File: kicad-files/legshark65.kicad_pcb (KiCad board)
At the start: 2 copper layers, 130 parts

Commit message: Update schematic to noLED MX only footpints
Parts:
- moved K_12 14.1 mm to (258.6, 30.0)
- moved K_26 14.1 mm to (258.6, 49.0)
- moved K_55 14.1 mm to (258.6, 96.7)
- moved K_41 14.1 mm to (258.6, 68.1)
- moved D_0 14.1 mm to (38.5, 30.5)
- moved D_1 14.1 mm to (57.6, 30.5)
- moved D_10 14.1 mm to (229.0, 30.5)
- moved D_11 14.1 mm to (248.1, 30.5)
- moved D_12 14.1 mm to (267.1, 30.5)
- moved D_13 14.1 mm to (286.2, 30.5)
- moved D_14 14.1 mm to (305.2, 30.5)
- moved D_15 14.1 mm to (57.6, 49.5)
- moved D_16 14.1 mm to (76.6, 49.5)
- moved D_17 14.1 mm to (95.7, 49.5)
- moved D_18 14.1 mm to (114.7, 49.5)
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
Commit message: Updated PCB design constraints
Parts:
- added C1: 15p, Capacitor_SMD:C_0603_1608Metric_Pad1.08x0.95mm_HandSolder, B.Cu at (245.9, 74.8)
- added C10: 100n, Capacitor_SMD:C_0603_1608Metric_Pad1.08x0.95mm_HandSolder, B.Cu at (153.6, 145.7)
- added C11: 100n, Capacitor_SMD:C_0603_1608Metric_Pad1.08x0.95mm_HandSolder, B.Cu at (153.6, 148.2)
- added C12: 10n, Capacitor_SMD:C_0603_1608Metric_Pad1.08x0.95mm_HandSolder, B.Cu at (153.6, 150.7)
- added C13: 4.7u, Capacitor_SMD:C_0603_1608Metric_Pad1.08x0.95mm_HandSolder, B.Cu at (149.2, 143.2)
- added C14: 100n, Capacitor_SMD:C_0603_1608Metric_Pad1.08x0.95mm_HandSolder, B.Cu at (149.2, 145.7)
- added C15: 4.7u, Capacitor_SMD:C_0603_1608Metric_Pad1.08x0.95mm_HandSolder, B.Cu at (149.2, 148.2)
- added C16: 16V 10uF Tantallum, acheron_Components:CP_EIA-3216-10_Kemet-I_Pad1.58x1.35mm_HandSolder, B.Cu at (155.1, 191.1)
- added C17: 100n, Capacitor_SMD:C_0603_1608Metric_Pad1.08x0.95mm_HandSolder, B.Cu at (149.2, 150.7)
- added C2: 15p, Capacitor_SMD:C_0603_1608Metric_Pad1.08x0.95mm_HandSolder, B.Cu at (245.9, 80.8)
- added C6: 100n, Capacitor_SMD:C_0603_1608Metric_Pad1.08x0.95mm_HandSolder, B.Cu at (237.6, 100.0)
- added C7: 100n, Capacitor_SMD:C_0603_1608Metric_Pad1.08x0.95mm_HandSolder, B.Cu at (157.9, 150.7)
- added C9: 100n, Capacitor_SMD:C_0603_1608Metric_Pad1.08x0.95mm_HandSolder, B.Cu at (153.6, 143.2)
- added Legshark_Logo2: Huge, Legshark:Legshark_Logo_Huge, F.Cu at (-74.8, 64.1)
- added R11: 100R, Resistor_SMD:R_0603_1608Metric, B.Cu at (158.1, 138.2)
- added R15: 10k, Resistor_SMD:R_0603_1608Metric, B.Cu at (158.1, 140.7)
- added R5: 1.5k, Resistor_SMD:R_0603_1608Metric, B.Cu at (158.1, 128.1)
- added R6: 10k, Resistor_SMD:R_0603_1608Metric, B.Cu at (158.1, 130.6)
- added R7: 4.7k, Resistor_SMD:R_0603_1608Metric, B.Cu at (245.0, 100.0)
- added R8: 4.7k, Resistor_SMD:R_0603_1608Metric, B.Cu at (241.3, 100.0)
- added SW1: K2-1187SQ-A4SW-06, acheron_Hardware:K2-1187SQ-A4SW-06, B.Cu at (155.3, 180.0)
- added SW2: PCM12SMTR, Legshark:Surface Mount Slide Switch SPDT, B.Cu at (155.2, 172.8)
- added SWD1: ~, Legshark:1x02_Long_Header, B.Cu at (152.2, 194.5)
- added T2: 53261-0471, Legshark:Molex, PicoBlade, 53261, 4 Way, 1 Row, Right Angle PCB Header, B.Cu at (154.0, 154.2)
- added U1: STM32F411CEU6, acheron_Components:STM_UFQFPN-48_LQFP-48-1EP_7x7mm_P0.5mm_HandSoldering, B.Cu at (258.0, 82.0)
- added U3: AT24C256C-SSHL-T, acheron_Components:TSSOP-8_4.4x3mm_P0.65mm, B.Cu at (241.3, 97.0)
- added Y1: TAXM8M4RFDCET2T, acheron_Components:Crystal_SMD_3225-4Pin_3.2x2.5mm, B.Cu at (245.9, 77.8)
- K_0, K_1, K_10, K_11, K_12, K_13, K_14, K_16, K_17, K_18, K_19, K_2, K_20, K_21, K_22, K_23, K_24, K_25, K_26, K_27, K_28, K_29, K_3, K_30, K_31, K_32, K_33, K_34, K_35, K_36, K_37, K_38, K_39, K_4, K_40, K_41, K_44, K_45, K_46, K_47, K_48, K_49, K_5, K_50, K_51, K_52, K_53, K_54, K_55, K_56, K_6, K_64, K_7, K_8, K_9: footprint MX_Alps_Hybrid:MX-1U-NoLED -> MX_Only:MXOnly-1U-NoLED
- K_15, K_42, K_43: footprint MX_Alps_Hybrid:MX-2U-NoLED -> MX_Only:MXOnly-2U-NoLED
- K_57: footprint MX_Alps_Hybrid:MX-1.75U-NoLED -> MX_Only:MXOnly-1.75U-NoLED
- K_58, K_59, K_62, K_63: footprint MX_Alps_Hybrid:MX-1.25U-NoLED -> MX_Only:MXOnly-1.25U-NoLED
- K_60: footprint MX_Alps_Hybrid:MX-2.25U-NoLED -> MX_Only:MXOnly-2.25U-ReversedStabilizers-NoLED
- K_61: footprint MX_Alps_Hybrid:MX-3U-NoLED -> MX_Only:MXOnly-3U-ReversedStabilizers-NoLED
- moved D_22 3.85 mm to (187.6, 51.5)
- moved D_26 3.85 mm to (263.8, 51.5)
- moved D_27 3.85 mm to (282.8, 51.5)
- moved D_28 3.85 mm to (301.9, 51.5)
- moved D_37 3.85 mm to (187.6, 70.5)
- moved D_41 3.85 mm to (263.8, 70.5)
- moved D_42 3.85 mm to (301.9, 70.5)
- moved D_55 3.85 mm to (263.8, 99.1)
- moved D_56 3.85 mm to (301.9, 99.1)
- moved K_20 3.85 mm to (140.9, 51.0)
- moved K_25 3.85 mm to (236.2, 51.0)
- moved K_26 3.85 mm to (255.2, 51.0)
- moved K_35 3.85 mm to (140.9, 70.0)
- moved K_40 3.85 mm to (236.2, 70.0)
- moved K_41 3.85 mm to (255.2, 70.0)
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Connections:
- net col0 renamed c0
- net col1 renamed c1
- net col10 renamed c10
- net col11 renamed c11
- net col12 renamed c12
- net col13 renamed c13
- net col14 renamed c14
- net col2 renamed c2
- net col3 renamed c3
- net col4 renamed c4
- net col5 renamed c5
- net col6 renamed c6
- net col7 renamed c7
- net col8 renamed c8
- net col9 renamed c9
- net row0 renamed r0
- net row1 renamed r1
- net row2 renamed r2
- net row3 renamed r3
- net row4 renamed r4
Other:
- board outline added: 290 x 92 mm
- rule pad_to_mask_clearance: 0 -> 0.1

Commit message: Connected most of the rows and cols
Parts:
- moved SW1 164.3 mm to (285.5, 79.8), turned to 90 degrees
- moved SW2 157.1 mm to (264.6, 60.1), turned to 0 degrees
- moved SWD1 155.1 mm to (245.9, 70.8), turned to -90 degrees
- moved C17 143.2 mm to (264.4, 65.7)
- moved C7 141.3 mm to (278.7, 77.4), turned to -90 degrees
- moved R11 136.9 mm to (280.8, 77.5), turned to -90 degrees
- moved C16 135.0 mm to (235.6, 82.7), turned to -90 degrees
- moved R15 131.1 mm to (264.4, 64.0), turned to 0 degrees
- moved C14 130.9 mm to (264.4, 83.5)
- moved C9 126.7 mm to (264.4, 81.8)
- moved C10 124.7 mm to (256.0, 74.7), turned to -90 degrees
- moved C12 117.1 mm to (254.8, 92.0)
- moved C13 116.6 mm to (254.8, 93.9)
- moved C15 115.2 mm to (248.4, 89.7), turned to -90 degrees
- moved C11 114.7 mm to (247.8, 82.8), turned to 0 degrees
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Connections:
- T2 pad 2: D+ -> D-
- T2 pad 3: D- -> D+
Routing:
- net r0: track 0.00 -> 257.2 mm
- net r4: track 0.00 -> 253.2 mm
- net r1: track 0.00 -> 247.6 mm
- net r2: track 0.00 -> 227.0 mm
- net r3: track 0.00 -> 191.5 mm
- net c0: track 0.00 -> 80.7 mm
- net c8: track 0.00 -> 80.4 mm
- net c10: track 0.00 -> 79.4 mm
- net c3: track 0.00 -> 77.3 mm
- net c2: track 0.00 -> 77.3 mm
- net c5: track 0.00 -> 77.3 mm
- net c1: track 0.00 -> 69.4 mm
- net c9: track 0.00 -> 57.2 mm
- net c7: track 0.00 -> 57.2 mm
- net c4: track 0.00 -> 57.2 mm
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- added copper zone on B.Cu, net (none)
- added copper zone on F.Cu, net (none)

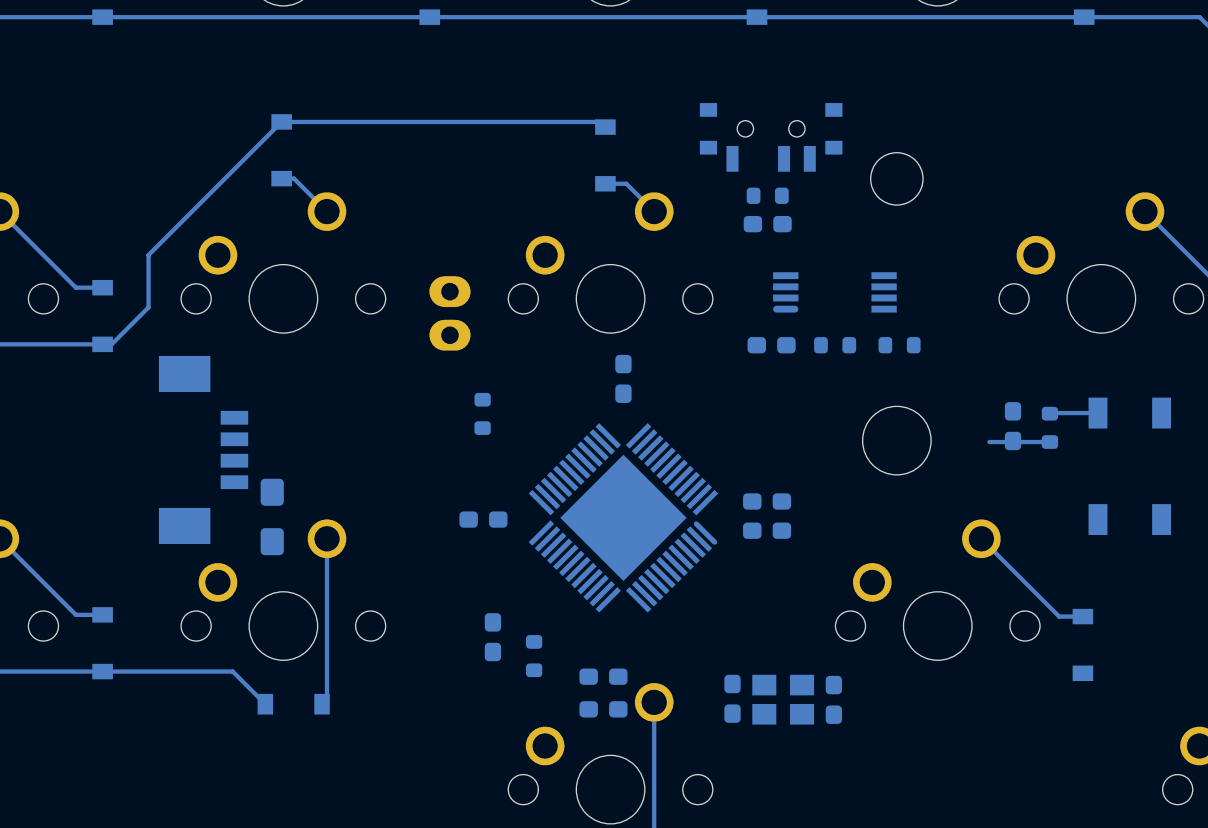
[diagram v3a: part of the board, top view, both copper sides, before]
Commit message: Started adding 3v3 pour
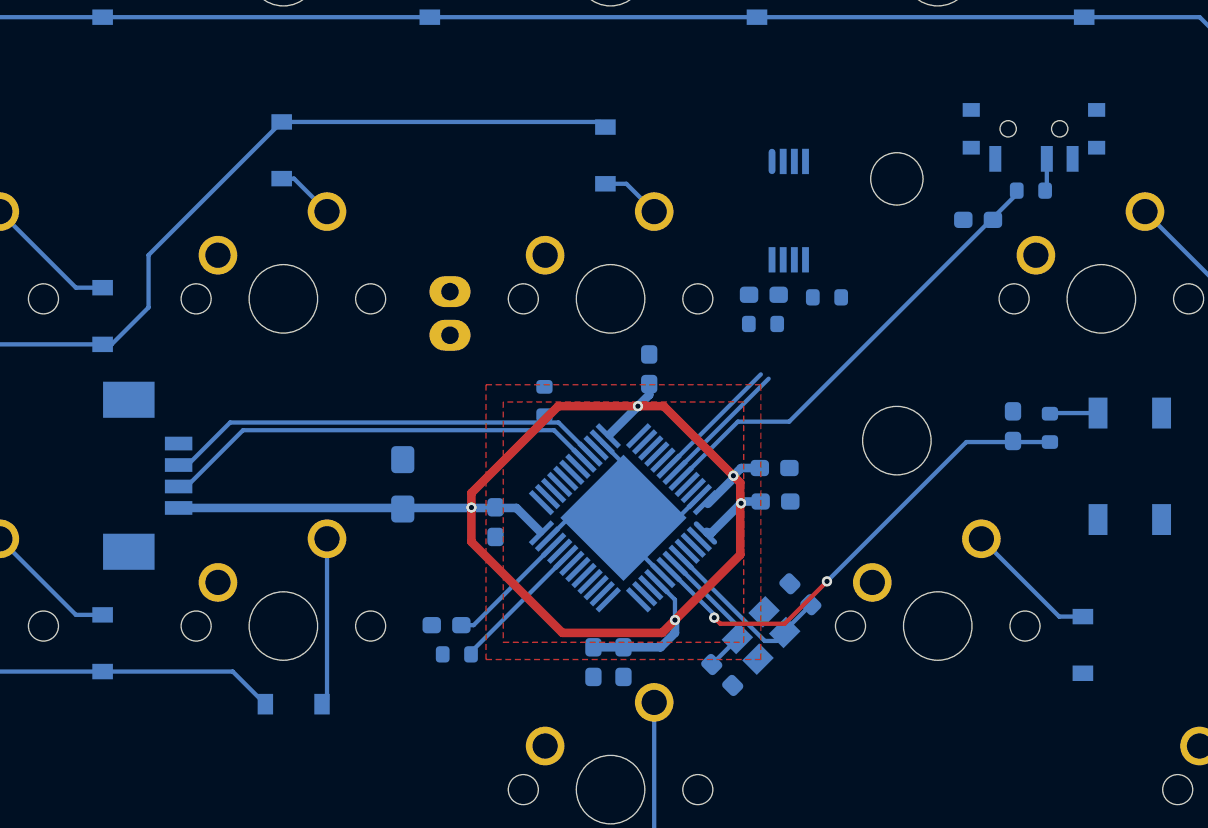
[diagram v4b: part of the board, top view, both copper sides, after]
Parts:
- moved R15 15.3 mm to (279.7, 63.7)
- moved SW2 15.3 mm to (279.9, 60.1)
- moved C17 12.3 mm to (276.6, 65.4), turned to 0 degrees
- moved C16 7.83 mm to (243.2, 80.8), turned to 90 degrees
- moved C2 6.45 mm to (266.3, 87.2), turned to 135 degrees
- moved U3 5.47 mm to (265.6, 64.9), turned to -90 degrees
- moved R7 5.06 mm to (267.9, 69.9)
- moved R6 4.50 mm to (246.3, 90.7), turned to 0 degrees
- moved R8 4.38 mm to (264.1, 71.5), turned to 0 degrees
- moved Y1 3.95 mm to (264.0, 89.6), turned to -135 degrees
- moved R5 3.68 mm to (251.4, 76.0)
- moved T2 3.58 mm to (229.3, 80.3)
- moved C6 2.97 mm to (264.2, 69.8)
- moved C13 2.81 mm to (254.2, 91.2), turned to 90 degrees
- moved C15 2.79 mm to (245.7, 89.0), turned to 180 degrees
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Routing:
- net 3V3: track 0.00 -> 88.4 mm, vias 0 -> 5
- net Net-(U1-BOOT0): track 0.00 -> 26.6 mm
- net D+: track 0.00 -> 25.2 mm
- net D-: track 0.00 -> 25.2 mm
- net Net-(U1-NRST): track 3.53 -> 28.0 mm, vias 0 -> 2
- net Net-(U1-PD0/OSC_IN): track 0.00 -> 10.5 mm
- net Net-(U1-PD1/OSC_OUT): track 0.00 -> 8.01 mm
- net Net-(U1-PB2--BOOT1): track 0.00 -> 7.94 mm
- net Net-(U1-PB7--I2C1_SDA): track 0.00 -> 7.71 mm
- net Net-(U1-PB6--I2C1_SCL): track 0.00 -> 7.56 mm
- net Net-(U1-VCAP_1): track 0.00 -> 7.30 mm
- net GND: track 0.00 -> 6.56 mm
- net Net-(SW2A-B): track 0.00 -> 1.89 mm
- added copper zone on F.Cu, net 3V3
- added copper zone on B.Cu, net GND
- added copper zone on F.Cu, net GND
- removed copper zone on B.Cu, net (none)
- removed copper zone on F.Cu, net (none)

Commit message: Created power pour on F and more wiring completion
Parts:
- moved C16 23.8 mm to (219.4, 79.8), turned to 180 degrees
- moved D_42 9.59 mm to (289.7, 61.6), turned to -90 degrees
- moved D_53 8.36 mm to (244.3, 90.0), turned to 90 degrees
- moved R8 4.68 mm to (265.6, 67.0), turned to 180 degrees
- moved U3 2.92 mm to (266.2, 62.0)
- moved C15 2.82 mm to (247.9, 87.3)
- moved C12 2.76 mm to (253.7, 92.6)
- moved C17 2.56 mm to (278.9, 64.1), turned to -90 degrees
- moved R6 2.41 mm to (248.1, 89.0)
- moved C11 1.97 mm to (246.6, 83.2)
- moved C13 1.79 mm to (255.2, 92.7)
- moved R7 1.36 mm to (266.5, 70.2)
- moved R15 1.31 mm to (280.9, 64.2), turned to 90 degrees
- moved C6 1.28 mm to (263.1, 69.2), turned to 90 degrees
- moved C9 1.23 mm to (265.5, 80.8)
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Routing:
- net c13: track 0.00 -> 77.5 mm
- net c11: track 0.00 -> 77.3 mm
- net c12: track 0.00 -> 72.5 mm
- net r3: track 191.5 -> 241.7 mm, vias 0 -> 2
- net r2: track 227.0 -> 264.2 mm
- net Net-(SWD1-SWCLK): track 0.00 -> 14.7 mm
- net Net-(SWD1-SWDIO): track 0.00 -> 13.0 mm
- net Net-(U1-PB7--I2C1_SDA): track 7.71 -> 18.6 mm
- net Net-(U1-PB6--I2C1_SCL): track 7.56 -> 18.1 mm
- net Net-(SW1-B): track 2.82 -> 9.02 mm
- net Net-(D_42-A): track 7.79 -> 4.03 mm
- net Net-(U1-VCAP_1): track 7.30 -> 4.35 mm
- net Net-(U1-PB2--BOOT1): track 7.94 -> 5.56 mm
- net Net-(D_53-A): track 9.75 -> 7.42 mm
- net Net-(U1-BOOT0): track 26.6 -> 28.0 mm
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
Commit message: Started connecting cols
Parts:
- moved SWD1 10.4 mm to (236.5, 75.2), turned to 0 degrees
- moved C13 6.78 mm to (261.9, 93.8)
- moved C12 6.56 mm to (260.2, 92.1)
- moved C1 3.91 mm to (265.8, 92.3), turned to 45 degrees
- moved R5 2.11 mm to (249.3, 76.1)
- moved SW1 1.44 mm to (286.2, 78.5), turned to 0 degrees
- moved R6 0.67 mm to (247.4, 88.9)
- moved D_54 0.20 mm to (282.8, 90.0)
- moved C11 0.15 mm to (246.6, 83.4)
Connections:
- U1 pad 2: unconnected-(U1-PC13-Pad2) -> r0
- U1 pad 21: C7 -> unconnected-(U1-PB10-Pad21)
- U1 pad 3: unconnected-(U1-PC14/OSC32_IN-Pad3) -> r4
- U1 pad 38: unconnected-(U1-PA15-Pad38) -> c12
- U1 pad 4: unconnected-(U1-PC15/OSC32_OUT-Pad4) -> r3
- U1 pad 40: unconnected-(U1-PB4-Pad40) -> c14
- U1 pad 41: unconnected-(U1-PB5-Pad41) -> c13
- U1 pad 45: unconnected-(U1-PB8-Pad45) -> r2
- U1 pad 46: unconnected-(U1-PB9-Pad46) -> r1
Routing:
- net c14: track 0.00 -> 100.6 mm, vias 0 -> 3
- net r0: track 257.2 -> 340.2 mm
- net unconnected-(U1-PB13/SPI2_SCK-Pad26): track 0.00 -> 70.0 mm, vias 0 -> 1
- net unconnected-(U1-PB14-Pad27): track 0.00 -> 68.4 mm, vias 0 -> 1
- net unconnected-(U1-PB15/SPI2_MOSI-Pad28): track 0.00 -> 67.5 mm, vias 0 -> 1
- net unconnected-(U1-PA8-Pad29): track 0.00 -> 67.0 mm, vias 0 -> 1
- net unconnected-(U1-PA10-Pad31): track 0.00 -> 67.0 mm, vias 0 -> 1
- net r1: track 247.6 -> 299.8 mm
- net r2: track 264.2 -> 312.7 mm
- net r4: track 253.2 -> 281.7 mm, vias 0 -> 2
- net unconnected-(U1-PB12-Pad25): track 0.00 -> 18.4 mm, vias 0 -> 1
- net r3: track 241.7 -> 256.8 mm, vias 2 -> 3
- net c13: track 77.5 -> 89.8 mm, vias 0 -> 1
- net Net-(SWD1-SWCLK): track 14.7 -> 24.7 mm
- net unconnected-(U1-PA3-Pad13): track 0.00 -> 7.46 mm
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
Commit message: Connected all of the wires of the new board
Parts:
- added R1: 51k, Resistor_SMD:R_0603_1608Metric, B.Cu at (247.5, 75.6)
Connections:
- U1 pad 13: unconnected-(U1-PA3-Pad13) -> c5
- U1 pad 14: unconnected-(U1-PA4-Pad14) -> c4
- U1 pad 15: unconnected-(U1-PA5-Pad15) -> c3
- U1 pad 16: unconnected-(U1-PA6-Pad16) -> c2
- U1 pad 17: unconnected-(U1-PA7-Pad17) -> c0
- U1 pad 18: unconnected-(U1-PB0-Pad18) -> c1
- U1 pad 25: unconnected-(U1-PB12-Pad25) -> c11
- U1 pad 27: unconnected-(U1-PB14-Pad27) -> c10
- U1 pad 28: unconnected-(U1-PB15/SPI2_MOSI-Pad28) -> c9
- U1 pad 29: unconnected-(U1-PA8-Pad29) -> c8
- U1 pad 31: unconnected-(U1-PA10-Pad31) -> c7
- U1 pad 39: unconnected-(U1-PB3-Pad39) -> c6
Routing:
- net c0: track 80.7 -> 312.5 mm
- net c1: track 69.4 -> 297.0 mm
- net c2: track 77.3 -> 280.7 mm
- net c3: track 77.3 -> 257.1 mm
- net c6: track 57.2 -> 231.3 mm, vias 0 -> 1
- net c4: track 57.2 -> 222.1 mm, vias 0 -> 1
- net c7: track 57.2 -> 209.3 mm, vias 0 -> 2
- net c5: track 77.3 -> 224.1 mm
- net c8: track 80.4 -> 210.4 mm, vias 0 -> 1
- net c9: track 57.2 -> 167.0 mm, vias 0 -> 1
- net c10: track 79.4 -> 168.6 mm, vias 0 -> 1
- net unconnected-(U1-PB13/SPI2_SCK-Pad26): track 70.0 -> 0.00 mm, vias 1 -> 0
- net unconnected-(U1-PB14-Pad27): track 68.4 -> 0.00 mm, vias 1 -> 0
- net unconnected-(U1-PB15/SPI2_MOSI-Pad28): track 67.5 -> 0.00 mm, vias 1 -> 0
- net unconnected-(U1-PA8-Pad29): track 67.0 -> 0.00 mm, vias 1 -> 0
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
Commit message: Lost of small changes to board
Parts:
- D_0, D_1, D_10, D_11, D_12, D_13, D_14, D_15, D_16, D_17, D_18, D_19, D_2, D_20, D_21, D_22, D_23, D_24, D_25, D_26, D_27, D_28, D_29, D_3, D_30, D_31, D_32, D_33, D_34, D_35, D_36, D_37, D_38, D_39, D_4, D_40, D_41, D_42, D_43, D_44, D_45, D_46, D_47, D_48, D_49, D_5, D_50, D_51, D_52, D_53, D_54, D_55, D_56, D_57, D_58, D_59, D_6, D_60, D_61, D_62, D_63, D_64, D_7, D_8, D_9: footprint Diode_SMD:D_SOD-123 -> acheron_Components:D_SOD-123
- moved C16 32.2 mm to (245.7, 98.4), turned to -90 degrees
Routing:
- net GND: track 6.56 -> 20.5 mm, vias 5 -> 12
- net unconnected-(U1-PA0-WKUP-Pad10): track 2.34 -> 0.00 mm
- net unconnected-(U1-PA1-Pad11): track 1.95 -> 0.00 mm
- net unconnected-(U1-PA2-Pad12): track 1.38 -> 0.00 mm
- net 3V3: track 88.8 -> 88.2 mm, vias 7 -> 8
